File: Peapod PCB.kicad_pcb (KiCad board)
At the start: 2 copper layers, 77.5 x 29 mm, 21 parts, among them J1 CONN_01X01, J2 CONN_01X01, J3 CONN_01X01, U1 ESP8266

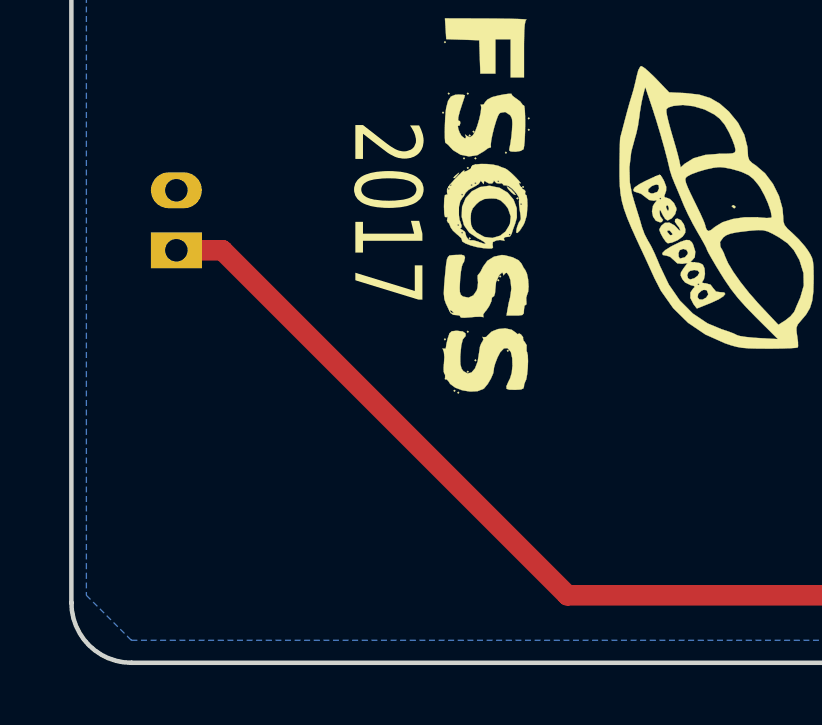
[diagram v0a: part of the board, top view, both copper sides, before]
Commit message: reversed pins on battery JST to reflect most common pinout
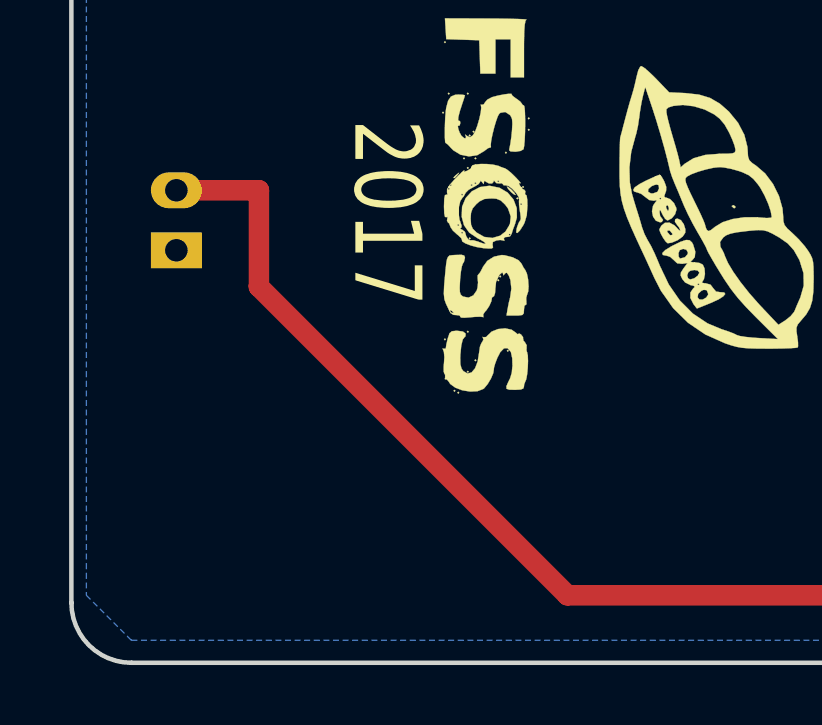
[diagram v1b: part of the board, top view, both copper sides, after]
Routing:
- net +3V3: track 140.1 -> 142.8 mm
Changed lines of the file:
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@@
     (links 32)
     (no_connects 0)
-    (area 91.424999 71.924999 169.075001 101.075001)
+    (area 79.900001 67.3 174.911943 103.638133)
     (thickness 1.6002)
     (drawings 41)
-    (tracks 103)
+    (tracks 104)
     (zones 0)
     (modules 21)
@@
     (add_net "Net-(R1-Pad1)")
     (add_net "Net-(U1-Pad1)")
+  )
+  (module Connectors_JST:JST_PH_B2B-PH-K_02x2.00mm_Straight (layer B.Cu)
+    (at 95 87.25 90)
+    (descr "JST PH series connector, B2B-PH-K, top entry type, through hole, Datasheet: http://www.jst-mfg.com/product/pdf/eng/ePH.pdf")
+    (tags "connector jst ph")
+    (fp_text reference BT1 (at 1.5 2.8 90) (layer B.SilkS) hide
+      (effects (font (size 1 1) (thickness 0.15)) (justify mirror))
+    )
+    (fp_text value Battery_Cell (at 1 -3.8 90) (layer B.Fab)
+      (effects (font (size 1 1) (thickness 0.15)) (justify mirror))
+    )
+    (fp_line (start -2.05 1.8) (end -2.05 -2.9) (layer B.SilkS) (width 0.12))
+    (fp_line (start -2.05 -2.9) (end 4.05 -2.9) (layer B.SilkS) (width 0.12))
+    (fp_line (start 4.05 -2.9) (end 4.05 1.8) (layer B.SilkS) (width 0.12))
+    (fp_line (start 4.05 1.8) (end -2.05 1.8) (layer B.SilkS) (width 0.12))
+    (fp_line (start 0.5 1.8) (end 0.5 1.2) (layer B.SilkS) (width 0.12))
+    (fp_line (start 0.5 1.2) (end -1.45 1.2) (layer B.SilkS) (width 0.12))
+    (fp_line (start -1.45 1.2) (end -1.45 -2.3) (layer B.SilkS) (width 0.12))
+    (fp_line (start -1.45 -2.3) (end 3.45 -2.3) (layer B.SilkS) (width 0.12))
+    (fp_line (start 3.45 -2.3) (end 3.45 1.2) (layer B.SilkS) (width 0.12))
+    (fp_line (start 3.45 1.2) (end 1.5 1.2) (layer B.SilkS) (width 0.12))
+    (fp_line (start 1.5 1.2) (end 1.5 1.8) (layer B.SilkS) (width 0.12))
+    (fp_line (start -2.05 0.5) (end -1.45 0.5) (layer B.SilkS) (width 0.12))
+    (fp_line (start -2.05 -0.8) (end -1.45 -0.8) (layer B.SilkS) (width 0.12))
+    (fp_line (start 4.05 0.5) (end 3.45 0.5) (layer B.SilkS) (width 0.12))
+    (fp_line (start 4.05 -0.8) (end 3.45 -0.8) (layer B.SilkS) (width 0.12))
+    (fp_line (start -0.3 1.8) (end -0.3 2) (layer B.SilkS) (width 0.12))
+    (fp_line (start -0.3 2) (end -0.6 2) (layer B.SilkS) (width 0.12))
+    (fp_line (start -0.6 2) (end -0.6 1.8) (layer B.SilkS) (width 0.12))
+    (fp_line (start -0.3 1.9) (end -0.6 1.9) (layer B.SilkS) (width 0.12))
+    (fp_line (start 0.9 -2.3) (end 0.9 -1.8) (layer B.SilkS) (width 0.12))
+    (fp_line (start 0.9 -1.8) (end 1.1 -1.8) (layer B.SilkS) (width 0.12))
+    (fp_line (start 1.1 -1.8) (end 1.1 -2.3) (layer B.SilkS) (width 0.12))
+    (fp_line (start 1 -2.3) (end 1 -1.8) (layer B.SilkS) (width 0.12))
+    (fp_line (start -1.1 2.1) (end -2.35 2.1) (layer B.SilkS) (width 0.12))
+    (fp_line (start -2.35 2.1) (end -2.35 0.85) (layer B.SilkS) (width 0.12))
+    (fp_line (start -1.1 2.1) (end -2.35 2.1) (layer B.Fab) (width 0.1))
+    (fp_line (start -2.35 2.1) (end -2.35 0.85) (layer B.Fab) (width 0.1))
+    (fp_line (start -1.95 1.7) (end -1.95 -2.8) (layer B.Fab) (width 0.1))
+    (fp_line (start -1.95 -2.8) (end 3.95 -2.8) (layer B.Fab) (width 0.1))
+    (fp_line (start 3.95 -2.8) (end 3.95 1.7) (layer B.Fab) (width 0.1))
+    (fp_line (start 3.95 1.7) (end -1.95 1.7) (layer B.Fab) (width 0.1))
+    (fp_line (start -2.45 2.2) (end -2.45 -3.3) (layer B.CrtYd) (width 0.05))
+    (fp_line (start -2.45 -3.3) (end 4.45 -3.3) (layer B.CrtYd) (width 0.05))
+    (fp_line (start 4.45 -3.3) (end 4.45 2.2) (layer B.CrtYd) (width 0.05))
+    (fp_line (start 4.45 2.2) (end -2.45 2.2) (layer B.CrtYd) (width 0.05))
+    (fp_text user %R (at 1 -1.5 90) (layer B.Fab)
+      (effects (font (size 1 1) (thickness 0.15)) (justify mirror))
+    )
+    (pad 2 thru_hole rect (at 0 0 90) (size 1.2 1.7) (drill 0.75) (layers *.Cu *.Mask)
+      (net 2 GND))
+    (pad 1 thru_hole oval (at 2 0 90) (size 1.2 1.7) (drill 0.75) (layers *.Cu *.Mask)
+      (net 1 +3V3))
+    (model ${KISYS3DMOD}/Connectors_JST.3dshapes/JST_PH_B2B-PH-K_02x2.00mm_Straight.wrl
+      (at (xyz 0 0 0))
+      (scale (xyz 1 1 1))
+      (rotate (xyz 0 0 0))
+    )
   )
   (module mod:star_1 (layer F.Cu)
@@
       (net 1 +3V3))
     (model Resistors_SMD.3dshapes/R_0805.wrl
-      (at (xyz 0 0 0))
-      (scale (xyz 1 1 1))
-      (rotate (xyz 0 0 0))
-    )
-  )
-  (module Connectors_JST:JST_PH_B2B-PH-K_02x2.00mm_Straight (layer B.Cu)
-    (at 95 87.25 90)
-    (descr "JST PH series connector, B2B-PH-K, top entry type, through hole, Datasheet: http://www.jst-mfg.com/product/pdf/eng/ePH.pdf")
-    (tags "connector jst ph")
-    (fp_text reference BT1 (at 1.5 2.8 90) (layer B.SilkS) hide
-      (effects (font (size 1 1) (thickness 0.15)) (justify mirror))
-    )
-    (fp_text value Battery_Cell (at 1 -3.8 90) (layer B.Fab)
-      (effects (font (size 1 1) (thickness 0.15)) (justify mirror))
-    )
-    (fp_line (start -2.05 1.8) (end -2.05 -2.9) (layer B.SilkS) (width 0.12))
-    (fp_line (start -2.05 -2.9) (end 4.05 -2.9) (layer B.SilkS) (width 0.12))
-    (fp_line (start 4.05 -2.9) (end 4.05 1.8) (layer B.SilkS) (width 0.12))
-    (fp_line (start 4.05 1.8) (end -2.05 1.8) (layer B.SilkS) (width 0.12))
-    (fp_line (start 0.5 1.8) (end 0.5 1.2) (layer B.SilkS) (width 0.12))
-    (fp_line (start 0.5 1.2) (end -1.45 1.2) (layer B.SilkS) (width 0.12))
-    (fp_line (start -1.45 1.2) (end -1.45 -2.3) (layer B.SilkS) (width 0.12))
-    (fp_line (start -1.45 -2.3) (end 3.45 -2.3) (layer B.SilkS) (width 0.12))
-    (fp_line (start 3.45 -2.3) (end 3.45 1.2) (layer B.SilkS) (width 0.12))
-    (fp_line (start 3.45 1.2) (end 1.5 1.2) (layer B.SilkS) (width 0.12))
-    (fp_line (start 1.5 1.2) (end 1.5 1.8) (layer B.SilkS) (width 0.12))
-    (fp_line (start -2.05 0.5) (end -1.45 0.5) (layer B.SilkS) (width 0.12))
-    (fp_line (start -2.05 -0.8) (end -1.45 -0.8) (layer B.SilkS) (width 0.12))
-    (fp_line (start 4.05 0.5) (end 3.45 0.5) (layer B.SilkS) (width 0.12))
-    (fp_line (start 4.05 -0.8) (end 3.45 -0.8) (layer B.SilkS) (width 0.12))
-    (fp_line (start -0.3 1.8) (end -0.3 2) (layer B.SilkS) (width 0.12))
-    (fp_line (start -0.3 2) (end -0.6 2) (layer B.SilkS) (width 0.12))
-    (fp_line (start -0.6 2) (end -0.6 1.8) (layer B.SilkS) (width 0.12))
-    (fp_line (start -0.3 1.9) (end -0.6 1.9) (layer B.SilkS) (width 0.12))
-    (fp_line (start 0.9 -2.3) (end 0.9 -1.8) (layer B.SilkS) (width 0.12))
-    (fp_line (start 0.9 -1.8) (end 1.1 -1.8) (layer B.SilkS) (width 0.12))
-    (fp_line (start 1.1 -1.8) (end 1.1 -2.3) (layer B.SilkS) (width 0.12))
-    (fp_line (start 1 -2.3) (end 1 -1.8) (layer B.SilkS) (width 0.12))
-    (fp_line (start -1.1 2.1) (end -2.35 2.1) (layer B.SilkS) (width 0.12))
-    (fp_line (start -2.35 2.1) (end -2.35 0.85) (layer B.SilkS) (width 0.12))
-    (fp_line (start -1.1 2.1) (end -2.35 2.1) (layer B.Fab) (width 0.1))
-    (fp_line (start -2.35 2.1) (end -2.35 0.85) (layer B.Fab) (width 0.1))
-    (fp_line (start -1.95 1.7) (end -1.95 -2.8) (layer B.Fab) (width 0.1))
-    (fp_line (start -1.95 -2.8) (end 3.95 -2.8) (layer B.Fab) (width 0.1))
-    (fp_line (start 3.95 -2.8) (end 3.95 1.7) (layer B.Fab) (width 0.1))
-    (fp_line (start 3.95 1.7) (end -1.95 1.7) (layer B.Fab) (width 0.1))
-    (fp_line (start -2.45 2.2) (end -2.45 -3.3) (layer B.CrtYd) (width 0.05))
-    (fp_line (start -2.45 -3.3) (end 4.45 -3.3) (layer B.CrtYd) (width 0.05))
-    (fp_line (start 4.45 -3.3) (end 4.45 2.2) (layer B.CrtYd) (width 0.05))
-    (fp_line (start 4.45 2.2) (end -2.45 2.2) (layer B.CrtYd) (width 0.05))
-    (fp_text user %R (at 1 -1.5 90) (layer B.Fab)
-      (effects (font (size 1 1) (thickness 0.15)) (justify mirror))
-    )
-    (pad 1 thru_hole rect (at 0 0 90) (size 1.2 1.7) (drill 0.75) (layers *.Cu *.Mask)
-      (net 1 +3V3))
-    (pad 2 thru_hole oval (at 2 0 90) (size 1.2 1.7) (drill 0.75) (layers *.Cu *.Mask)
-      (net 2 GND))
-    (model ${KISYS3DMOD}/Connectors_JST.3dshapes/JST_PH_B2B-PH-K_02x2.00mm_Straight.wrl
       (at (xyz 0 0 0))
       (scale (xyz 1 1 1))
@@
     (effects (font (size 1 1) (thickness 0.2)) (justify mirror))
   )
+  (segment (start 97.75 85.25) (end 95 85.25) (width 0.6858) (layer F.Cu) (net 1))
+  (segment (start 139.25 98.75) (end 108.0358 98.75) (width 0.6858) (layer F.Cu) (net 1))
+  (segment (start 108.0358 98.75) (end 97.75 88.4642) (width 0.6858) (layer F.Cu) (net 1))
+  (segment (start 97.75 88.4642) (end 97.75 85.25) (width 0.6858) (layer F.Cu) (net 1))
   (segment (start 156 79.5) (end 156 82.25) (width 0.6858) (layer F.Cu) (net 1))
   (segment (start 161.5 85) (end 161.5 95.75) (width 0.6858) (layer F.Cu) (net 1))
@@
   (segment (start 148.915862 92.15) (end 143.5858 92.15) (width 0.6858) (layer F.Cu) (net 1))
   (segment (start 143.5858 92.15) (end 142.25 92.15) (width 0.6858) (layer F.Cu) (net 1))
-  (segment (start 139.25 98.75) (end 108.0358 98.75) (width 0.6858) (layer F.Cu) (net 1))
   (segment (start 142.25 92.15) (end 140.9142 92.15) (width 0.6858) (layer F.Cu) (net 1))
   (segment (start 140.9142 92.15) (end 139.25 93.8142) (width 0.6858) (layer F.Cu) (net 1))
   (segment (start 139.25 93.8142) (end 139.25 98.75) (width 0.6858) (layer F.Cu) (net 1))
-  (segment (start 108.0358 98.75) (end 96.5358 87.25) (width 0.6858) (layer F.Cu) (net 1))
-  (segment (start 96.5358 87.25) (end 95 87.25) (width 0.6858) (layer F.Cu) (net 1))
   (segment (start 155.5 76.75) (end 156 77.25) (width 0.6858) (layer F.Cu) (net 1))
   (segment (start 156 77.25) (end 156 79.5) (width 0.6858) (layer F.Cu) (net 1))
